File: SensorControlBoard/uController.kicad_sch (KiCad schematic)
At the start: 42 parts, among them J10 Conn_01x05_Pin, J11 USB_C_Receptacle_USB2.0, J2 Conn_01x02_Pin, J5 Conn_01x10_Pin, J6 Conn_01x02_Pin, J7 Conn_01x02_Pin, J8 Conn_01x02_Pin, SW1 SW_SPDT, U1 STM32F103C8T6TR, U2 TLV1117LV33DCYR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

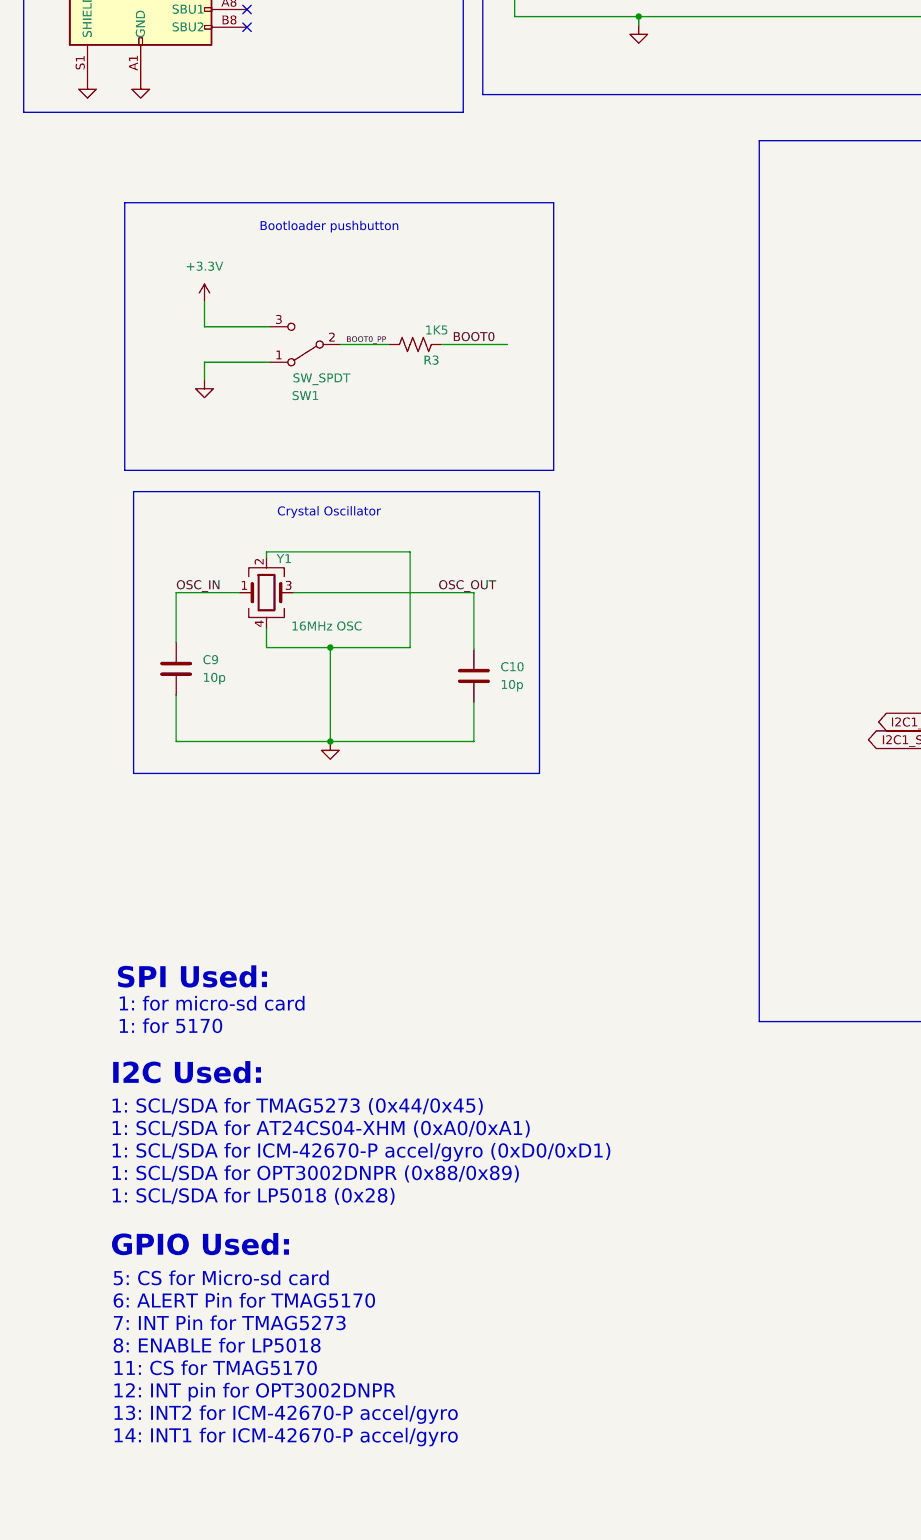
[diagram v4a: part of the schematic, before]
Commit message: added TVS protection diodes
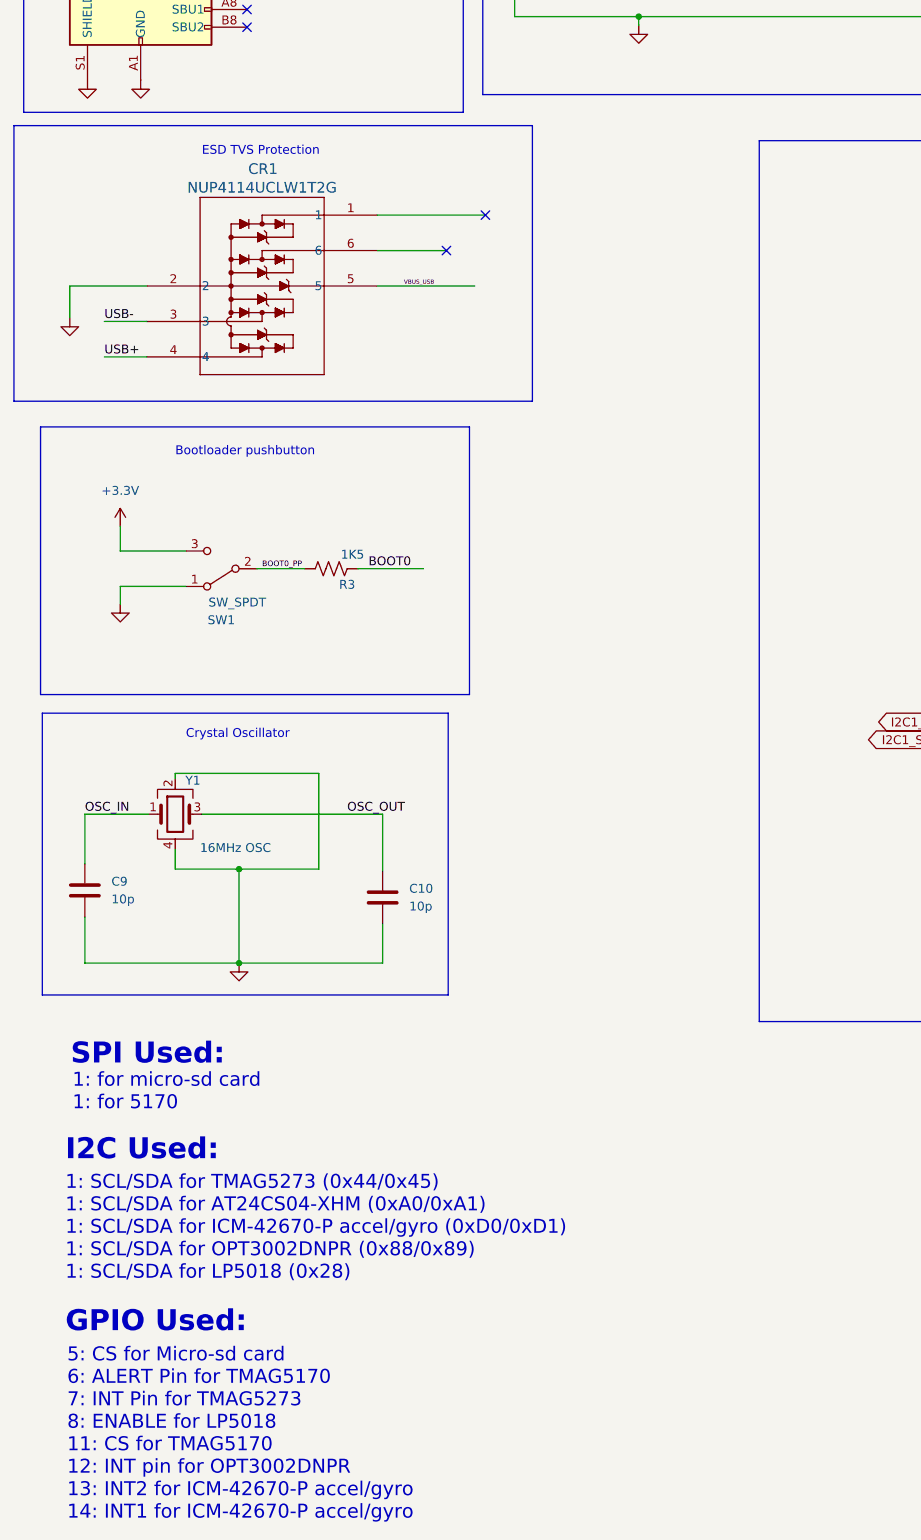
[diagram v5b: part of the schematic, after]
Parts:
- added CR1: NUP4114UCLW1T2G, NUP4114:SC-88&slash_SC70-6&slash_SOT-363_419B-02_ONS_OSI-M, symbol NUP4114:NUP4114UCLW1T2G
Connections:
- net GND: now also CR1.2
- net USB+: now also CR1.4
- net USB-: now also CR1.3
- net VBUS_USB: now also CR1.5
- no-connect marks 6 -> 8
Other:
- note added: "ESD TVS Protection"
- moved on the sheet: C10, C9, R3, SW1, Y1

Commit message: A0 PCB Commit
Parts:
- C1, C2, C3, C8: MP C0805C104K5RAC7210 -> C0603C104M4RAC7411
- C10, C9: MP C0805C100F3HAC7800 -> C0603C100J1GACTU
- C11, C6, C7: MP C0805C105Z4VAC7800 -> C0603C105K4RACTU
- C4: MP C0805C106K8PAC7800 -> C0603C106M9PACTU
- C5: MP C0805C103K1RAC7800 -> C0603C103M2RECAUTO
- CR1: MP (none) -> NUP4114UCLW1T2G
- FB1: MP 2508051217Y6 -> BLM18KG121TN1D
- J10, J2, J5, J6, J7, J8: MP (none) -> 61304011121
- J11: MP (none) -> 12402012E212A
- U1: MP (none) -> STM32F103C8T6TR
- Y1: MP (none) -> ABM11-16.000MHZ-D2X-T3
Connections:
- net +3.3V: no longer J5.2 (Pin_2), J5.4 (Pin_4)
- net GND: now also J5.4 (Pin_4); no longer J5.3 (Pin_3)
- net GPIO_10: now also J5.2 (Pin_2)
- net GPIO_2: now also J5.3 (Pin_3)
- net GPIO_3: now also J5.4 (Pin_4)
- no-connect marks 8 -> 7
